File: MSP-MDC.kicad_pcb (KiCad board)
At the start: 2 copper layers, 106.7 x 106.7 mm, 40 parts, among them U10 74LS00, U11 74LS32, U12 74LS86, U13 74LS166, U14 74LS374, U15 74LS138, U16 74LS257, U17 74LS257, U18 74LS257, U19 74LS257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

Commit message: Import routing for the first revision
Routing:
- net /BUF_D0: track 0.00 -> 192.6 mm, vias 0 -> 4
- net /Top Board/A7: track 0.00 -> 185.6 mm, vias 0 -> 8
- net /Top Board/A5: track 0.00 -> 174.6 mm, vias 0 -> 9
- net /Top Board/A3: track 0.00 -> 164.4 mm, vias 0 -> 5
- net /Top Board/A10: track 0.00 -> 161.8 mm, vias 0 -> 5
- net /BUF_D1: track 0.00 -> 159.4 mm, vias 0 -> 4
- net /Top Board/A4: track 0.00 -> 146.3 mm, vias 0 -> 3
- net /Top Board/A1: track 0.00 -> 145.1 mm, vias 0 -> 4
- net /BUF_D6: track 0.00 -> 144.6 mm, vias 0 -> 5
- net /BUF_D7: track 0.00 -> 143.4 mm, vias 0 -> 3
- net /BUF_D2: track 0.00 -> 142.9 mm, vias 0 -> 7
- net /J1-4: track 0.00 -> 138.0 mm, vias 0 -> 2
- net /BUF_D3: track 0.00 -> 132.0 mm, vias 0 -> 5
- net /J3-18: track 0.00 -> 127.5 mm, vias 0 -> 1
- net /Top Board/Mid Board/D6: track 0.00 -> 126.0 mm
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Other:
- board text added: "- REDUX -"
- board text added: "Rev. 0"

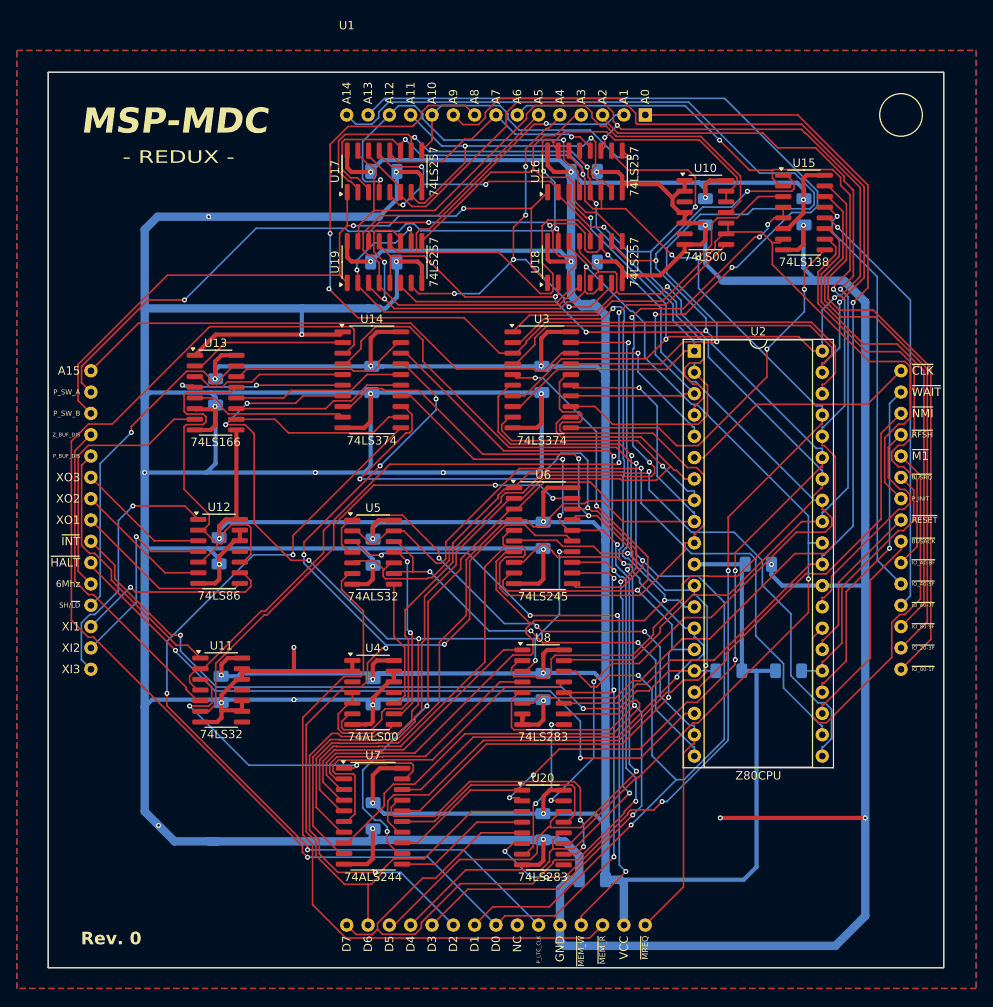
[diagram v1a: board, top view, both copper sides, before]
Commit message: Reduce size of the board to match original
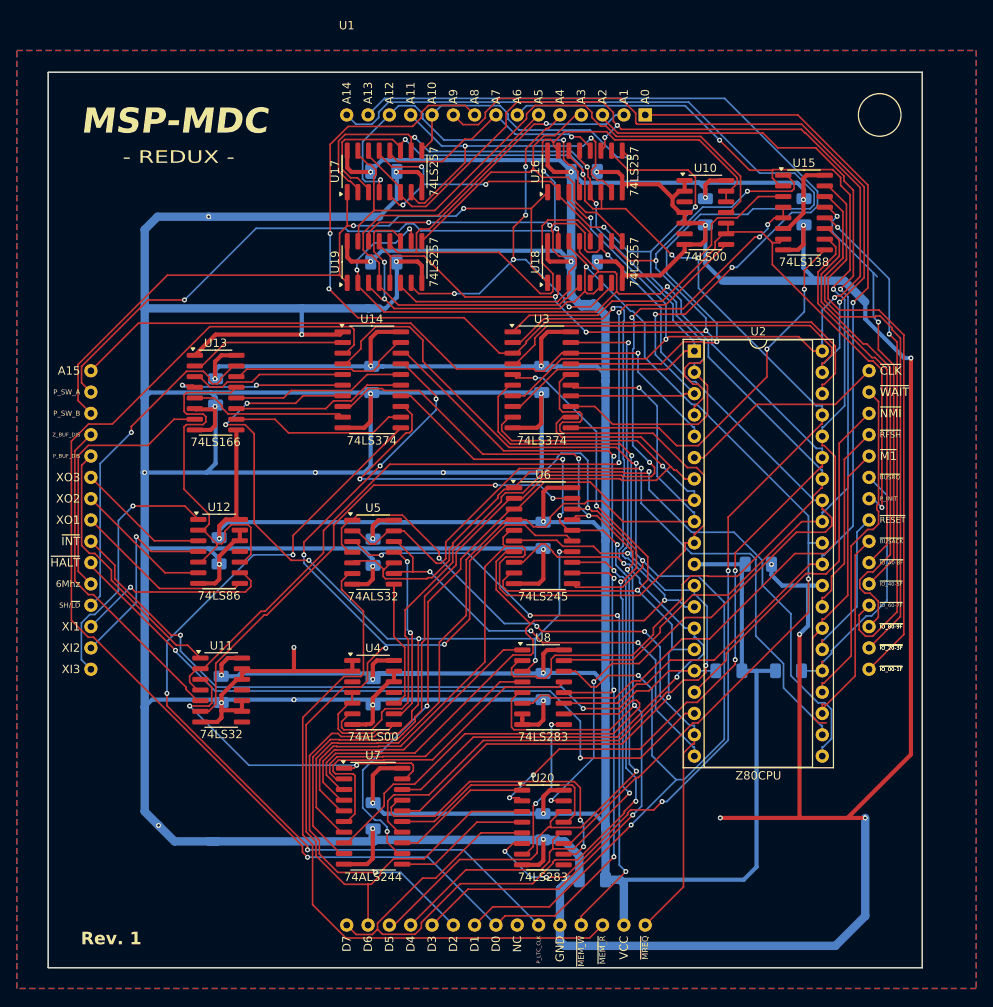
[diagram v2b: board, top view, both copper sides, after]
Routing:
- net GND: track 791.5 -> 819.4 mm, vias 28 -> 30
- net /J1-14: track 50.7 -> 36.7 mm
- net /J1-22: track 51.1 -> 60.2 mm, vias 1 -> 2
- net /J1-24: track 51.2 -> 44.7 mm
- net /J1-13: track 27.4 -> 23.5 mm
- net /J3-20: track 28.9 -> 25.1 mm
- net /J2-10: track 102.8 -> 105.7 mm
- net /Top Board/A10: track 161.8 -> 164.3 mm
- net /Top Board/Mid Board/~{IO_R}: track 15.5 -> 17.5 mm
- net /J1-1: track 81.7 -> 79.9 mm, vias 0 -> 1
- net /J2-3: track 44.9 -> 43.3 mm
- net /J1-21: track 49.4 -> 50.9 mm, vias 1 -> 2
- net /J1-23: track 57.8 -> 56.5 mm
- net /J1-11: track 125.4 -> 126.5 mm
- net /Top Board/A4: track 146.3 -> 147.4 mm
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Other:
- board size 106.7 x 106.7 mm -> 104.1 x 106.7 mm
- board text added: "Rev. 1"
- board text added: "~{IO_00-1F}"
- board text added: "~{IO_20-3F}"
- board text added: "~{IO_80-9F}"
- board text removed: "Rev. 0"

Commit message: Resize the board
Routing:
- net /J1-24: track 44.7 -> 60.3 mm
- net GND: track 819.4 -> 827.8 mm, vias 30 -> 28
- net /J1-21: track 50.9 -> 54.6 mm, vias 2 -> 0
- net /J1-22: track 60.2 -> 56.6 mm, vias 2 -> 0
- net /J1-16: track 31.8 -> 28.4 mm
- net /J1-1: track 79.9 -> 77.8 mm, vias 1 -> 0
- net /J1-20: track 63.9 -> 62.4 mm
- net /J3-20: track 25.1 -> 26.6 mm, vias 0 -> 1
- net /J1-19: track 68.0 -> 66.6 mm
- net /J1-8: track 114.6 -> 113.8 mm
- net /J1-23: track 56.5 -> 55.7 mm
- net /Top Board/A4: track 147.4 -> 146.8 mm
- net /J1-11: track 126.5 -> 126.0 mm
- net /Top Board/A5: track 175.7 -> 175.2 mm
- net /Top Board/A7: track 186.7 -> 186.2 mm
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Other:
- board text removed: "~{IO_00-1F}"
- board text removed: "~{IO_20-3F}"
- board text removed: "~{IO_80-9F}"

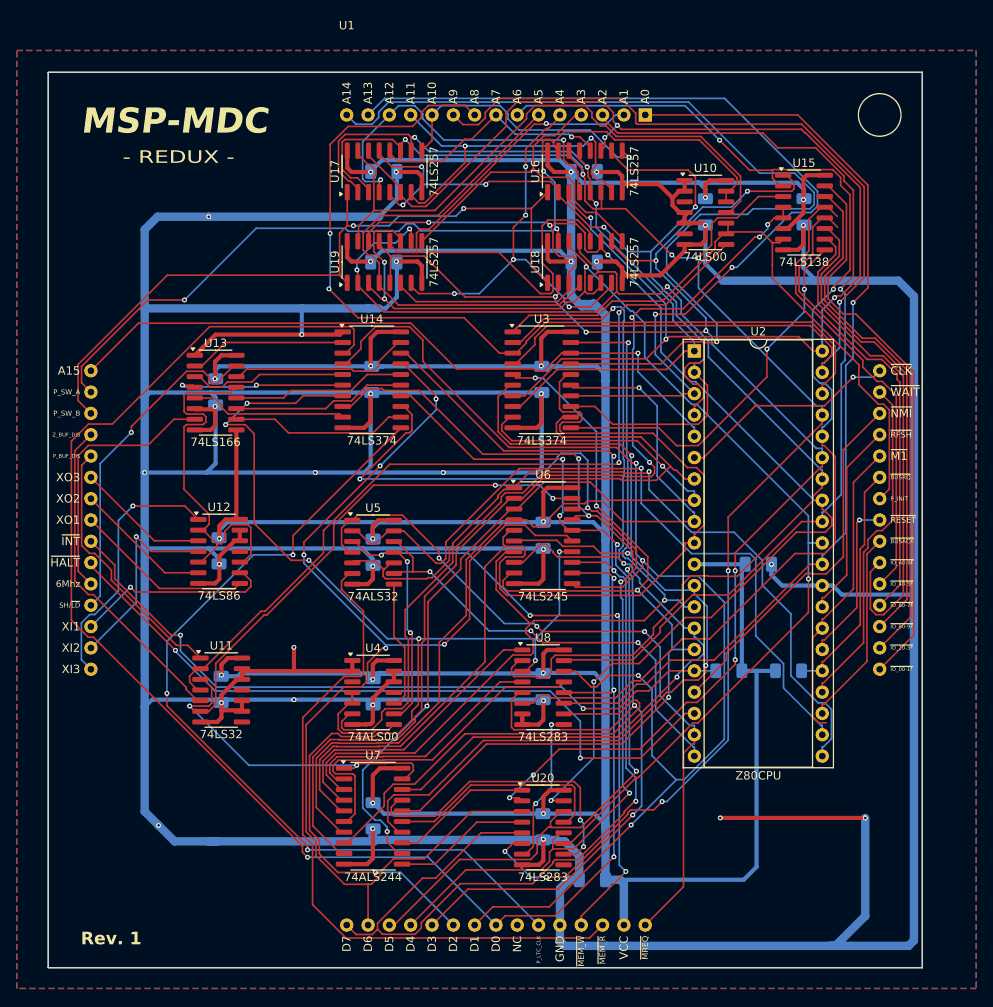
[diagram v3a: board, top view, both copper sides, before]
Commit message: Update board fixing adder issues
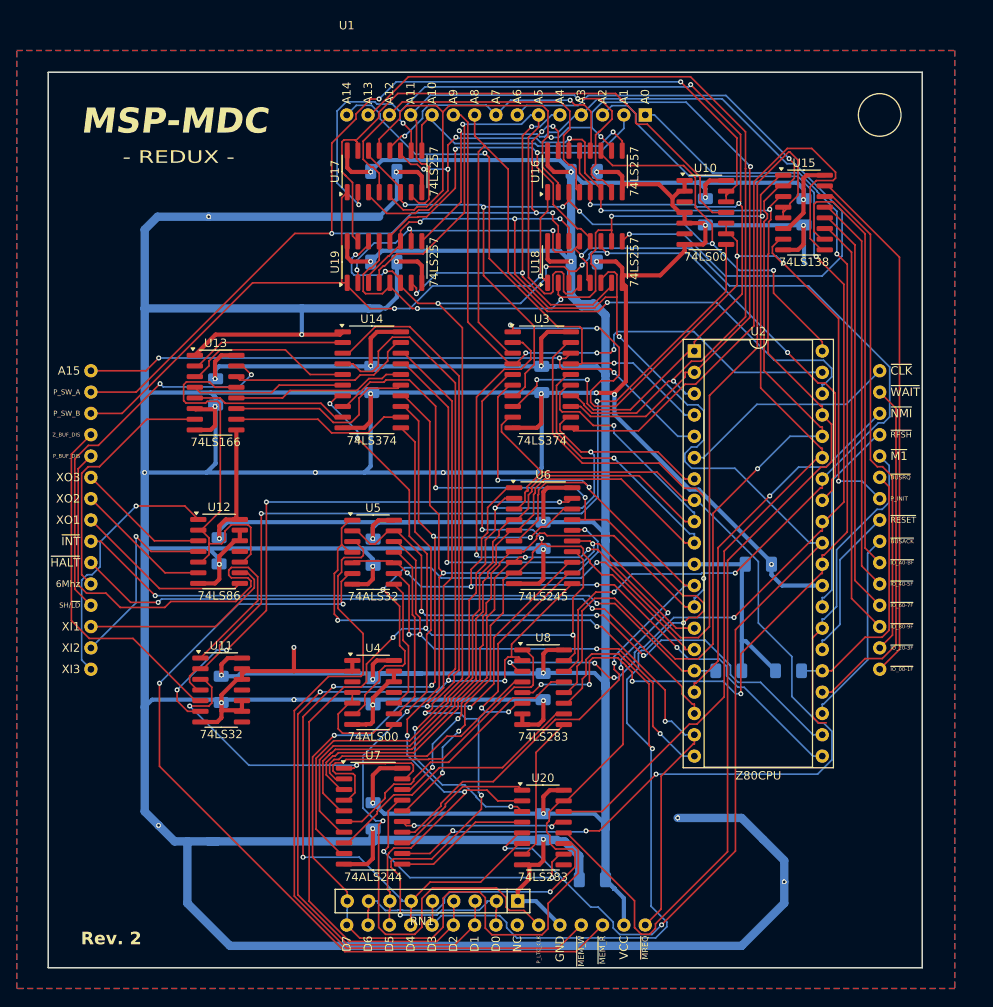
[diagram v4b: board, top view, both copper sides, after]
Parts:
- added RN1: 10K, Resistor_THT:R_Array_SIP9, F.Cu at (125.7, 129.3)
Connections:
- U20 pad 11: /Top Board/A1 -> /BUF_D7
- U20 pad 12: /BUF_D4 -> /Top Board/A7
- U20 pad 14: /BUF_D5 -> /Top Board/A5
- U20 pad 15: /Top Board/A3 -> /BUF_D6
- U20 pad 2: /Top Board/A5 -> /BUF_D5
- U20 pad 3: /BUF_D6 -> /Top Board/A3
- U20 pad 5: /BUF_D7 -> /Top Board/A1
- U20 pad 6: /Top Board/A7 -> /BUF_D4
- U8 pad 11: /J1-10 -> /BUF_D3
- U8 pad 12: /BUF_D0 -> /J1-4
- U8 pad 14: /BUF_D1 -> /Top Board/A4
- U8 pad 15: /J1-8 -> /BUF_D2
- U8 pad 2: /Top Board/A4 -> /BUF_D1
- U8 pad 3: /BUF_D2 -> /J1-8
- U8 pad 5: /BUF_D3 -> /J1-10
- U8 pad 6: /J1-4 -> /BUF_D0
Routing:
- net /J1-7: track 42.4 -> 103.5 mm, vias 0 -> 2
- net /Top Board/A11: track 94.8 -> 154.8 mm, vias 3 -> 7
- net /J3-18: track 128.1 -> 68.4 mm, vias 1 -> 2
- net /BUF_D0: track 192.6 -> 139.9 mm, vias 4 -> 5
- net /J1-11: track 126.0 -> 74.9 mm, vias 1 -> 3
- net /Top Board/A10: track 164.1 -> 116.8 mm, vias 5 -> 6
- net /J2-8: track 111.5 -> 156.5 mm, vias 3 -> 7
- net /Top Board/A1: track 145.1 -> 183.5 mm, vias 4 -> 6
- net /BUF_D3: track 132.0 -> 167.2 mm, vias 5 -> 4
- net GND: track 827.8 -> 796.7 mm, vias 28 -> 30
- net /Top Board/~{IO_ACCESS}: track 105.5 -> 135.7 mm, vias 4 -> 2
- net VCC: track 623.6 -> 594.1 mm
- net /J3-15: track 31.5 -> 59.4 mm
- net /Top Board/Mid Board/D3: track 105.0 -> 129.3 mm
- net /Top Board/Mid Board/D0: track 120.0 -> 96.1 mm, vias 3 -> 5
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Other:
- board text added: "Rev. 2"
- board text removed: "Rev. 1"
